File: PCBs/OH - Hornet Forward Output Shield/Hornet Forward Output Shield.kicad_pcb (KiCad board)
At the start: 2 copper layers, 97.9 x 53.3 mm, 21 parts, among them J1 MATRIX INPUT, J10 DIGITAL B, J11 DIGITAL C, J2 5V to Max7219, J3 7219 OUT, J4 ANALOG B, J6 ANALOG A, J7 Address Select 0, J8 Address Select 1, J9 DIGITAL A, P1 Power, P2 Analog, P3 Analog, P4 Digital, P5 PWM, P6 PWM, P7 Communication

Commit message: PCBS
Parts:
- added J12: LEFT SERVO, PT_Library_v001:Molex_1x03_P2.54mm_Vertical, F.Cu at (190.0, 88.2)
- added J13: RIGHT OUTPUT DIST, PT_Library_v001:Molex_1x06_P2.54mm_Vertical, F.Cu at (172.7, 88.2)
- added J14: LEFT STEPPER, PT_Library_v001:Molex_1x04_P2.54mm_Vertical, F.Cu at (200.2, 80.4)
- added J5: LEFT OUTPUT DIST, PT_Library_v001:Molex_1x10_P2.54mm_Vertical, F.Cu at (172.7, 80.4)
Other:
- board text added: "HORNET FORWARD OUTPUT"
- board text removed: "HORNET FORWARD INPUT"

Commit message: PCBS
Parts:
- removed J10: DIGITAL B, PT_Library_v001:Molex_1x06_P2.54mm_Vertical
- removed J11: DIGITAL C, PT_Library_v001:Molex_1x06_P2.54mm_Vertical
- removed J9: DIGITAL A, PT_Library_v001:Molex_1x06_P2.54mm_Vertical
- J1: value MATRIX INPUT -> OUTPUT
- J4: value ANALOG B -> RIGHT SERVO; footprint PT_Library_v001:Molex_1x10_P2.54mm_Vertical -> PT_Library_v001:Molex_1x06_P2.54mm_Vertical
- J5: footprint PT_Library_v001:Molex_1x10_P2.54mm_Vertical -> PT_Library_v001:Molex_1x08_P2.54mm_Vertical
- J6: value ANALOG A -> RIGHT STEPPER; footprint PT_Library_v001:Molex_1x10_P2.54mm_Vertical -> PT_Library_v001:Molex_1x04_P2.54mm_Vertical
- moved J2 63.3 mm to (190.2, 77.6)
- moved J12 62.3 mm to (128.8, 99.9)
- moved J4 55.9 mm to (128.1, 89.7), turned to 0 degrees
- moved J6 49.0 mm to (208.7, 113.5), turned to 0 degrees
- moved J5 45.1 mm to (217.0, 88.8), turned to 90 degrees
- moved J3 39.4 mm to (172.8, 77.6)
- moved J1 28.6 mm to (235.6, 73.7)
- moved J13 25.8 mm to (185.3, 110.7), turned to 90 degrees
- moved J14 15.6 mm to (206.9, 94.5)
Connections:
- J1 pad 10: /30 -> (no net)
- J1 pad 11: /31 -> (no net)
- J1 pad 12: /32 -> (no net)
- J1 pad 13: /33 -> (no net)
- J1 pad 14: /34 -> (no net)
- J1 pad 15: /35 -> (no net)
- J1 pad 16: /36 -> (no net)
- J1 pad 17: /37 -> (no net)
- J1 pad 18: /38 -> (no net)
- J1 pad 19: /39 -> (no net)
- J1 pad 2: /22 -> (no net)
- J1 pad 20: /40 -> (no net)
- J1 pad 21: /41 -> (no net)
- J1 pad 22: /42 -> (no net)
- J1 pad 23: /43 -> (no net)
- J1 pad 24: /44 -> (no net)
- J1 pad 25: /45 -> (no net)
- J1 pad 26: /46 -> (no net)
- J1 pad 27: /47 -> (no net)
- J1 pad 28: /48 -> (no net)
- J1 pad 3: /23 -> (no net)
- J1 pad 4: /24 -> (no net)
- J1 pad 5: /25 -> (no net)
- J1 pad 6: /26 -> (no net)
- J1 pad 7: /27 -> (no net)
- J1 pad 8: /28 -> (no net)
- J1 pad 9: /29 -> (no net)
- J12 pad 1: (no net) -> /D12
- J12 pad 2: (no net) -> +5VL
- J12 pad 3: (no net) -> GNDD
- J13 pad 1: (no net) -> /22
- J13 pad 2: (no net) -> /23
- J13 pad 3: (no net) -> /24
- J13 pad 4: (no net) -> /25
- J13 pad 6: (no net) -> GND
- J14 pad 1: (no net) -> /39
- J14 pad 2: (no net) -> /37
- J14 pad 3: (no net) -> /35
- J14 pad 4: (no net) -> /33
- J2 pad 1: +5VL -> +5V
- J3 pad 2: GNDD -> GND
- J3 pad 3: /D9 -> /16(Tx2)
- J3 pad 4: /D8 -> /15(Rx3)
- J3 pad 5: /D7 -> /14(Tx3)
- J4 pad 1: +5V -> /D11
- J4 pad 2: GND -> /D9
- J4 pad 3: /A8 -> /D8
- J4 pad 4: /A9 -> /D7
- J4 pad 5: /A10 -> /D6
- J4 pad 6: /A11 -> GNDD
- J5 pad 1: (no net) -> /26
- J5 pad 2: (no net) -> /27
- J5 pad 3: (no net) -> /28
- J5 pad 4: (no net) -> /29
- J5 pad 5: (no net) -> /30
- J5 pad 6: (no net) -> /31
- J5 pad 8: (no net) -> GND
- J6 pad 1: +5VL -> /47
- J6 pad 2: GNDD -> /45
- J6 pad 3: /A0 -> /43
- J6 pad 4: /A1 -> /41
- P2 pad 1: /A0 -> (no net)
- P2 pad 2: /A1 -> (no net)
- P2 pad 3: /A2 -> (no net)
- P2 pad 4: /A3 -> (no net)
- P2 pad 5: /A4 -> (no net)
- P2 pad 6: /A5 -> (no net)
- P3 pad 1: /A8 -> (no net)
- P3 pad 2: /A9 -> (no net)
- P3 pad 3: /A10 -> (no net)
- P3 pad 4: /A11 -> (no net)
- P3 pad 5: /A12 -> (no net)
- P3 pad 6: /A13 -> (no net)
- P3 pad 7: /A14 -> (no net)
- P3 pad 8: /A15 -> (no net)
- P4 pad 11: /44 -> (no net)
- P4 pad 13: /42 -> (no net)
- P4 pad 15: /40 -> (no net)
- P4 pad 17: /38 -> (no net)
- P4 pad 19: /36 -> (no net)
- P4 pad 21: /34 -> (no net)
- P4 pad 23: /32 -> (no net)
- P4 pad 7: /48 -> (no net)
- P4 pad 9: /46 -> (no net)
- P5 pad 3: /D13 -> (no net)
- P6 pad 3: /D5 -> (no net)
- P6 pad 7: /D1 -> (no net)
- P6 pad 8: /D0 -> (no net)
- P7 pad 1: (no net) -> /14(Tx3)
- P7 pad 2: (no net) -> /15(Rx3)
- P7 pad 3: (no net) -> /16(Tx2)
- P7 pad 4: (no net) -> /17(Rx2)
- P7 pad 5: (no net) -> /18(Tx1)
- R12 pad 1: /D5 -> /17(Rx2)
- R13 pad 1: /D6 -> /18(Tx1)

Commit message: PCBS
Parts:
- added J10: I2C, PT_Library_v001:Molex_1x04_P2.54mm_Vertical, F.Cu at (179.7, 94.7)
- added J11: NEXTION, PT_Library_v001:Molex_1x04_P2.54mm_Vertical, F.Cu at (204.2, 73.4)
- added J9: PIXEL LEDS, PT_Library_v001:Molex_1x08_P2.54mm_Vertical, F.Cu at (173.1, 112.1)
- J1: value OUTPUT -> CABIN ALT; footprint Connector_IDC:IDC-Header_2x17_P2.54mm_Vertical -> PT_Library_v001:Molex_1x04_P2.54mm_Vertical
- J14: value LEFT STEPPER -> BRAKE PRESSURE
- J6: value RIGHT STEPPER -> RADAR ALT
- J7, J8: footprint PT_Library_v001:Molex_1x02_P2.54mm_Vertical -> Connector_PinHeader_2.54mm:PinHeader_1x02_P2.54mm_Vertical
- moved J1 40.9 mm to (208.3, 104.1)
- moved D1 19.8 mm to (161.7, 97.9)
- moved D2 19.8 mm to (161.8, 103.1)
- moved R12 19.8 mm to (161.9, 93.9)
- moved R13 19.8 mm to (161.8, 107.8)
- moved J13 9.45 mm to (179.1, 103.6), turned to 0 degrees
- moved J8 7.98 mm to (149.9, 77.9)
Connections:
- net /D2 renamed /ADDRESS_SELECT_0
- net /D3 renamed /ADDRESS_SELECT_1
- J1 pad 1: (no net) -> /32
- J1 pad 2: (no net) -> /34
- J1 pad 3: (no net) -> /36
- J1 pad 4: (no net) -> /38
- P4 pad 11: (no net) -> /44
- P4 pad 13: (no net) -> /42
- P4 pad 15: (no net) -> /40
- P4 pad 17: (no net) -> /38
- P4 pad 19: (no net) -> /36
- P4 pad 21: (no net) -> /34
- P4 pad 23: (no net) -> /32
- P4 pad 7: (no net) -> /48
- P4 pad 8: (no net) -> /49
- P4 pad 9: (no net) -> /46
- P5 pad 3: (no net) -> /D13
- P6 pad 3: (no net) -> /D5
- P7 pad 4: /17(Rx2) -> (no net)
- P7 pad 6: (no net) -> /19(Rx1)
- P7 pad 7: (no net) -> /20(SDA)
- P7 pad 8: (no net) -> /21(SCL)
- R12 pad 1: /17(Rx2) -> /D13
- R13 pad 1: /18(Tx1) -> /D5

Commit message: PCBS
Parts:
- added J15: 5V IN, Connector_BarrelJack:BarrelJack_Horizontal, F.Cu at (140.3, 106.8)
- added J16: UPPER 5V OUT, PT_Library_v001:Molex_1x02_P2.54mm_Vertical, F.Cu at (161.8, 110.6)
- J2: value 5V to Max7219 -> LOWER 5V IN
- J4: value RIGHT SERVO -> RIGHT_SERVO; footprint PT_Library_v001:Molex_1x06_P2.54mm_Vertical -> PT_Library_v001:Molex_1x08_P2.54mm_Vertical
- moved J2 37.6 mm to (172.3, 110.6)
- moved R12 35.5 mm to (132.5, 74.0)
- moved R13 32.9 mm to (164.5, 75.1)
- moved D1 18.4 mm to (164.5, 79.8)
- moved D2 18.4 mm to (164.6, 85.0)
- moved J9 17.4 mm to (173.9, 94.7)
- moved J7 10.8 mm to (156.7, 75.1), turned to 90 degrees
- moved J10 10.4 mm to (184.8, 85.6)
- moved J4 10.2 mm to (127.5, 79.5)
- moved J12 9.12 mm to (131.3, 91.2)
- moved J13 7.00 mm to (179.6, 110.6)
- moved J8 2.84 mm to (149.4, 75.1), turned to 90 degrees
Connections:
- J10 pad 1: +5V -> /LOWER_OUTPUT_5V
- J11 pad 1: +5V -> /LOWER_OUTPUT_5V
- J12 pad 2: +5VL -> /UPPER_OUTPUT_5V
- J2 pad 1: +5V -> /LOWER_OUTPUT_5V
- J2 pad 2: Net-(J2-Pad2) -> GND
- J3 pad 1: Net-(J2-Pad2) -> /LOWER_OUTPUT_5V
- J4 pad 1: /D11 -> /UPPER_OUTPUT_5V
- J4 pad 2: /D9 -> GNDD
- J4 pad 3: /D8 -> /D11
- J4 pad 4: /D7 -> /D9
- J4 pad 5: /D6 -> /D8
- J4 pad 6: GNDD -> /D7
- P1 pad 5: +5VL -> (no net)

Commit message: PCBS
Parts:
- added J15: ANALOG, PT_Library_v001:Molex_1x06_P2.54mm_Vertical, F.Cu at (153.7, 112.5)
- R1: renamed from R12; value R -> 330
- R2: renamed from R13; value R -> 330
- moved J7 36.0 mm to (172.1, 89.5)
- moved J1 19.7 mm to (207.8, 71.4), turned to 270 degrees
- moved J9 17.8 mm to (174.4, 112.5)
- moved R2 10.2 mm to (154.3, 74.9)
- moved J17 9.44 mm to (150.2, 84.5)
- moved J16 9.38 mm to (158.1, 84.3)
- moved J2 9.17 mm to (180.2, 101.5)
- moved J6 7.08 mm to (162.9, 103.6)
- moved J5 6.83 mm to (173.5, 103.9)
- moved J3 4.22 mm to (127.4, 89.7)
- moved D1 3.19 mm to (164.7, 76.6)
- moved J13 2.77 mm to (209.6, 95.2)
- moved J14 2.57 mm to (209.6, 116.0)
- moved D2 2.03 mm to (164.6, 82.9)
- moved J12 1.94 mm to (209.6, 105.6)
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- renumbered J5 to J1, J15 to J11, J1 to J12, J14 to J13, J6 to J14, J7 to J16, J8 to J17, J13 to J2, J12 to J3, J2 to J5, J16 to J6, J11 to J7, J3 to J8
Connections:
- P1 pad 5: (no net) -> +5VL
- P2 pad 1: (no net) -> /A0
- P2 pad 2: (no net) -> /A1
- P2 pad 3: (no net) -> /A2
- P2 pad 4: (no net) -> /A3
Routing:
- net GNDD: track 0.00 -> 124.5 mm
- net GND: track 0.00 -> 123.4 mm
- net /UPPER_OUTPUT_5V: track 0.00 -> 53.8 mm
- net /LOWER_OUTPUT_5V: track 0.00 -> 39.4 mm
- net /23: track 0.00 -> 36.6 mm
- net /22: track 0.00 -> 35.4 mm
- net Net-(D1-Pad2): track 0.00 -> 33.9 mm
- net /25: track 0.00 -> 32.0 mm
- net /24: track 0.00 -> 31.4 mm
- net /40: track 0.00 -> 30.5 mm
- net /36: track 0.00 -> 28.2 mm
- net /41: track 0.00 -> 27.8 mm
- net /42: track 0.00 -> 27.2 mm
- net /32: track 0.00 -> 26.8 mm
- net /D12: track 0.00 -> 25.6 mm
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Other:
- net class GND AND POWER added: clearance 0.2, trace_width 0.45, via_dia 0.6, via_drill 0.4
- board text added: "5V"
- board text added: "APU"
- board text added: "BLEED"
- board text added: "CANOPY"
- board text added: "CLK"
- board text added: "DATA"
- board text added: "ENG CRANK"
- board text added: "FUEL DUMP"
- board text added: "GND"
- board text added: "HOOK BYPASS"
- board text added: "LAND GEAR"
- board text added: "LASER"
- board text added: "LAUNCH BAR"
- board text added: "LOD"
- board text added: "PITOT"
- board text added: "RX"
- board text added: "SCL"
- board text added: "SDA"
- board text added: "STEPPERS"
- board text added: "TX"

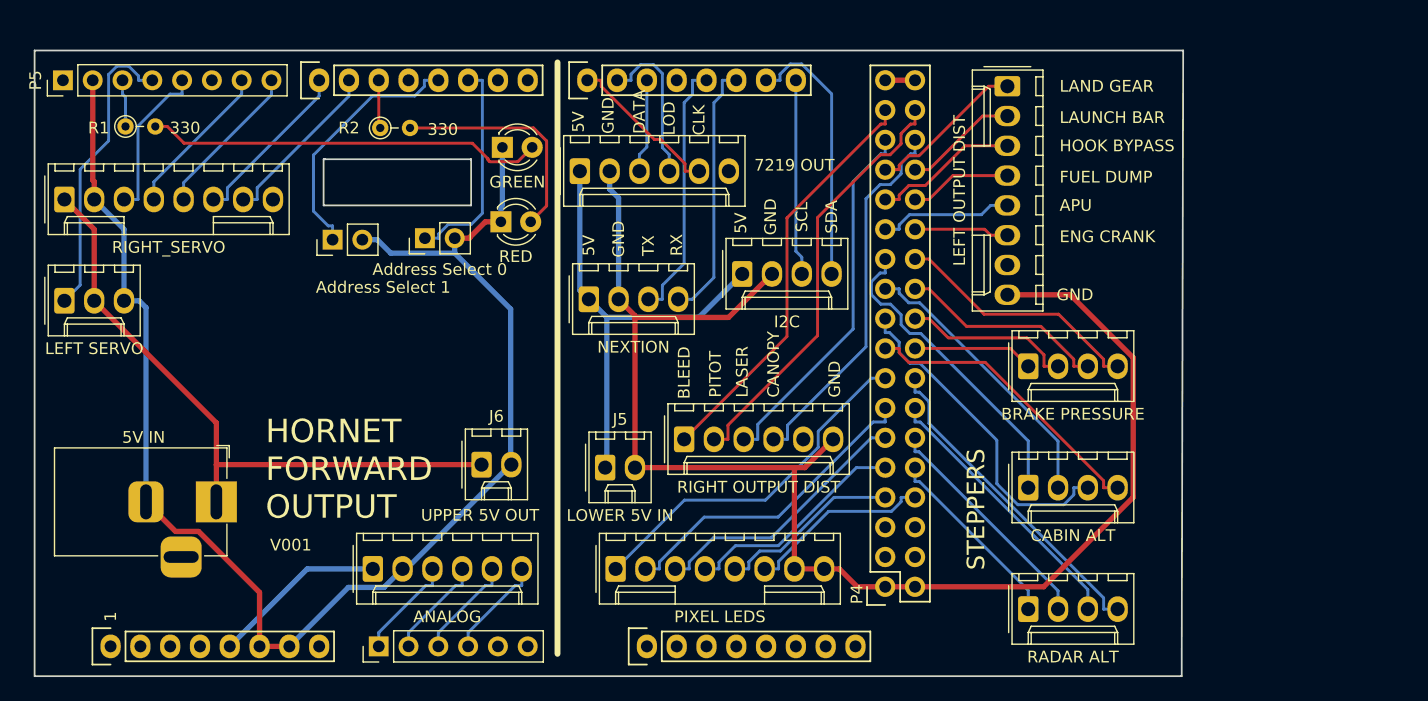
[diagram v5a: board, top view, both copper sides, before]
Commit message: ALL ORDERED ASIDE FROM FORWARD INPUT
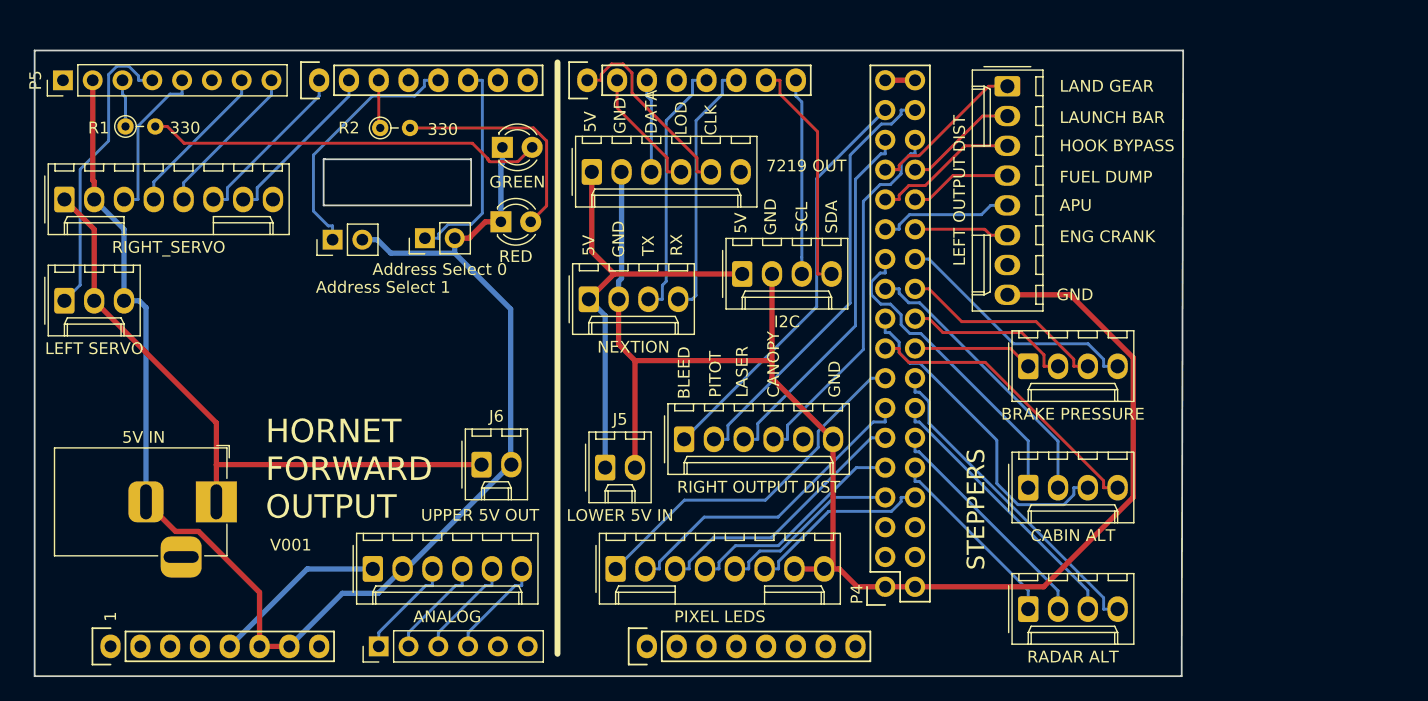
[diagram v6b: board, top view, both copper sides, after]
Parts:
- moved J8 1.02 mm to (172.3, 78.7)
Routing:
- net /14(Tx3): track 13.4 -> 16.9 mm
- net /15(Rx3): track 13.6 -> 10.8 mm
- net /20(SDA): track 22.9 -> 20.2 mm
- net GND: track 123.4 -> 122.5 mm
- net /LOWER_OUTPUT_5V: track 39.4 -> 38.4 mm
- net /23: track 36.6 -> 37.1 mm

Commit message: ALL PCBS ORDERED
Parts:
- added J18: NEXTION ANA, PT_Library_v001:Molex_1x03_P2.54mm_Vertical, F.Cu at (144.8, 112.5)
- moved R1 13.5 mm to (146.1, 74.0)
- moved J3 4.76 mm to (127.3, 94.4)
- moved J4 2.29 mm to (127.3, 83.3)
- moved J5 2.17 mm to (173.2, 101.7)
- moved J6 2.03 mm to (163.0, 101.6)
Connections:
- P2 pad 5: (no net) -> /A4
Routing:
- net /A4: track 0.00 -> 20.3 mm
- net Net-(D1-Pad2): track 33.9 -> 20.8 mm
- net /D13: track 4.04 -> 15.2 mm
- net /D12: track 25.6 -> 31.1 mm
- net +5VL: track 14.9 -> 18.1 mm
- net /D7: track 14.6 -> 17.6 mm
- net GNDD: track 124.5 -> 127.3 mm
- net /D9: track 13.3 -> 15.6 mm
- net /D8: track 13.3 -> 15.6 mm
- net /LOWER_OUTPUT_5V: track 38.4 -> 36.1 mm
- net /D6: track 14.6 -> 16.2 mm
- net /36: track 28.2 -> 27.0 mm
- net /D11: track 13.5 -> 14.5 mm
- net GND: track 122.5 -> 123.3 mm
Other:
- board text added: "40"
- board text added: "42"
- board text added: "44"
- board text added: "46"
- board text added: "48"
- board text added: "49"
- board text added: "A0"
- board text added: "A1"
- board text added: "A2"
- board text added: "A3"
- board text added: "ALT-FLAG"
- board text added: "BATT_E"
- board text added: "BATT_U"
- board text added: "HYD_P_1"
- board text added: "HYD_P_2"
- board text added: "NEXTION A4"
- board text added: "TRIM"

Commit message: PCB
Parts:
- moved J8 5.14 mm to (177.5, 78.7)
- moved J7 3.62 mm to (174.9, 87.3)
- moved J5 2.11 mm to (174.8, 100.3)
- moved J2 1.43 mm to (181.0, 100.3)
- moved J9 1.09 mm to (175.4, 112.4)
- moved J10 1.02 mm to (186.2, 87.3)
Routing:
- net /15(Rx3): track 10.8 -> 17.1 mm
- net GND: track 123.3 -> 118.6 mm
- net /14(Tx3): track 16.9 -> 21.4 mm
- net /34: track 24.3 -> 28.4 mm
- net /19(Rx1): track 22.1 -> 18.0 mm
- net /18(Tx1): track 22.1 -> 18.0 mm
- net /LOWER_OUTPUT_5V: track 36.1 -> 33.7 mm
- net /16(Tx2): track 7.97 -> 10.1 mm
- net /36: track 27.0 -> 29.0 mm
- net /22: track 35.6 -> 33.6 mm
- net /25: track 32.0 -> 30.4 mm
- net /24: track 31.4 -> 29.9 mm
- net /21(SCL): track 16.7 -> 17.9 mm
- net /48: track 15.7 -> 14.6 mm
- net /42: track 27.2 -> 26.0 mm
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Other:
- board text added: "V002"
- board text removed: "V001"
